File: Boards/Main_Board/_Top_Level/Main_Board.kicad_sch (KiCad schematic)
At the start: 4 parts, among them J2 OQ0212500000G, J3 OQ0432500000G, J4 OQ0432500000G, J5 OQ0432500000G

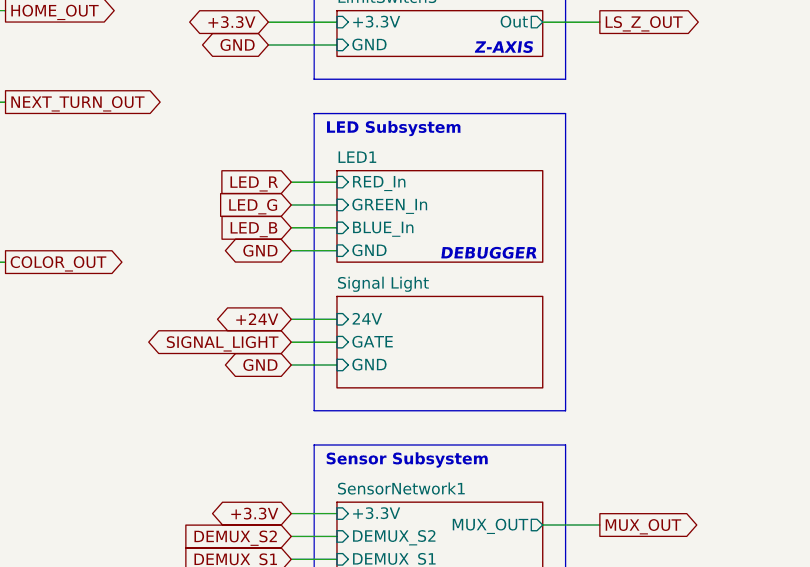
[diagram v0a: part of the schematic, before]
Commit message: Correct spacing on sensor board, refactor datasheets and project libraries
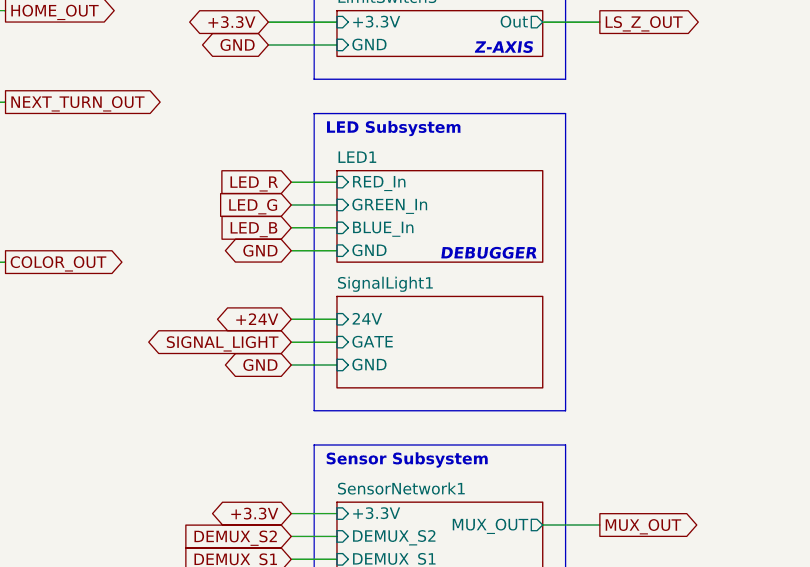
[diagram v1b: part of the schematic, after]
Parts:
- J3, J4, J5: symbol OQ04325500000G:OQ0432500000G -> OQ0432500000G:OQ0432500000G
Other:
- sheet Signal Light renamed SignalLight1
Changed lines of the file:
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@@
     )
   )
-  (symbol (lib_id "OQ04325500000G:OQ0432500000G") (at 254 100.33 0) (unit 1)
+  (symbol (lib_id "OQ0432500000G:OQ0432500000G") (at 254 100.33 0) (unit 1)
     (in_bom yes) (on_board yes) (fields_autoplaced)
     (property "Reference" "J5" (id 0) (at 270.51 102.8699 0)
@@
       (effects (font (size 1.27 1.27)) hide)
     )
-    (property "Manufacturer's Part Number" "OQ0432500000G" (id 14) (at 254 100.33 0)
-      (effects (font (size 1.27 1.27)) hide)
+    (property "Manufacturer's Part Number" "OQ0432500000G" (id 14) (at 270.51 115.57 0)
+      (effects (font (size 1.27 1.27)) (justify left) hide)
     )
     (pin "1")
@@
     (pin "4")
   )
-  (symbol (lib_id "OQ04325500000G:OQ0432500000G") (at 254 38.1 0) (unit 1)
+  (symbol (lib_id "OQ0432500000G:OQ0432500000G") (at 254 38.1 0) (unit 1)
     (in_bom yes) (on_board yes) (fields_autoplaced)
     (property "Reference" "J3" (id 0) (at 270.51 40.6399 0)
@@
       (effects (font (size 1.27 1.27)) hide)
     )
-    (property "Manufacturer's Part Number" "OQ0432500000G" (id 14) (at 254 38.1 0)
-      (effects (font (size 1.27 1.27)) hide)
+    (property "Manufacturer's Part Number" "OQ0432500000G" (id 14) (at 270.51 53.34 0)
+      (effects (font (size 1.27 1.27)) (justify left) hide)
     )
     (pin "1")
@@
     (pin "2")
   )
-  (symbol (lib_id "OQ04325500000G:OQ0432500000G") (at 254 68.58 0) (unit 1)
+  (symbol (lib_id "OQ0432500000G:OQ0432500000G") (at 254 68.58 0) (unit 1)
     (in_bom yes) (on_board yes) (fields_autoplaced)
     (property "Reference" "J4" (id 0) (at 270.51 71.1199 0)
@@
       (effects (font (size 1.27 1.27)) hide)
     )
-    (property "Manufacturer's Part Number" "OQ0432500000G" (id 14) (at 254 68.58 0)
-      (effects (font (size 1.27 1.27)) hide)
+    (property "Manufacturer's Part Number" "OQ0432500000G" (id 14) (at 270.51 83.82 0)
+      (effects (font (size 1.27 1.27)) (justify left) hide)
     )
     (pin "1")
@@
     (stroke (width 0.1524) (type solid) (color 0 0 0 0))
     (fill (color 0 0 0 0.0000))
-    (property "Sheet name" "Signal Light" (id 0) (at 149.86 74.2184 0)
+    (property "Sheet name" "SignalLight1" (id 0) (at 149.86 74.2184 0)
       (effects (font (size 1.27 1.27)) (justify left bottom))
     )

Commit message: Fix typos
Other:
- sheet MSP432E401Y ports: added PD_6; removed PA_6
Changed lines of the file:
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@@
       (effects (font (size 1.27 1.27)) (justify right))
     )
-    (pin "PA_6" bidirectional (at 63.5 107.95 90)
+    (pin "PD_6" bidirectional (at 63.5 107.95 90)
       (effects (font (size 1.27 1.27)) (justify right))
     )
